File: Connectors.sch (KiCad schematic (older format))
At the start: 4 parts, among them J2 I2C connector, J3 Digital pins, J4 Serial connector, J5 ICSP connector

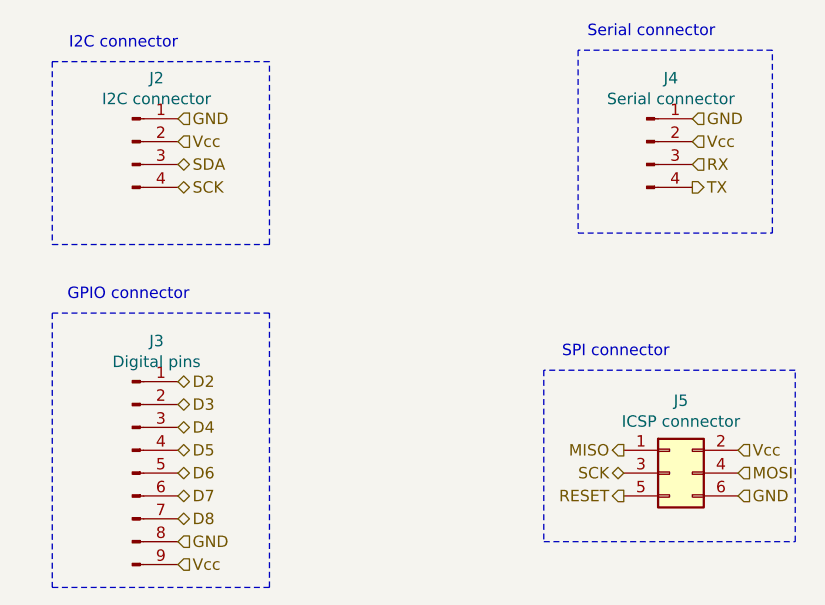
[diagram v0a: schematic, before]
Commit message: Adjusted designators, units etc as per Larry's feedback.
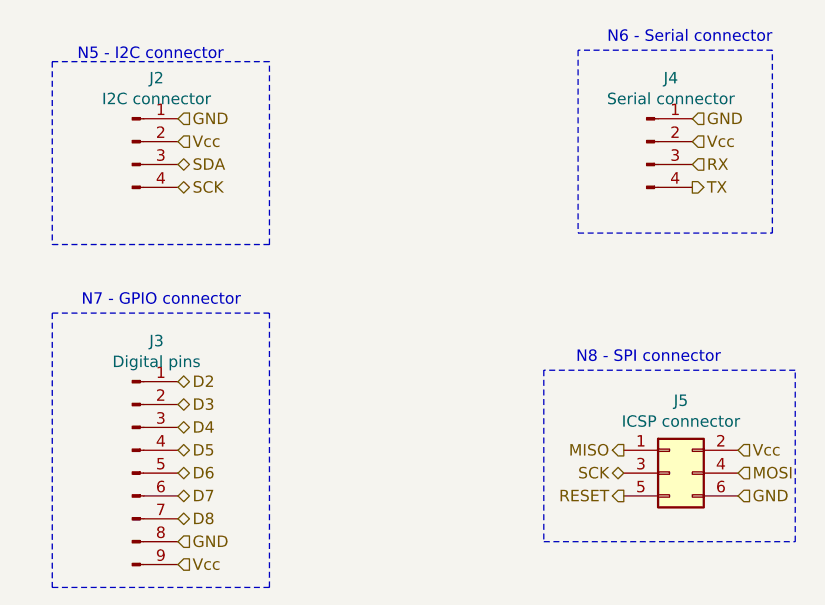
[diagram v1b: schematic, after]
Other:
- note added: "N5 - I2C connector"
- note added: "N6 - Serial connector"
- note added: "N7 - GPIO connector"
- note added: "N8 - SPI connector"
- note removed: "GPIO connector"
- note removed: "I2C connector"
- note removed: "SPI connector"
- note removed: "Serial connector"
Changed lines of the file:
@@
 EESchema Schematic File Version 4
+LIBS:BACEE-cache
 EELAYER 26 0
 EELAYER END
@@
 Wire Notes Line
 	6600 3500 5500 3500
-Text Notes 3900 2100 2    50   ~ 0
-I2C connector
-Text Notes 6250 2050 2    50   ~ 0
-Serial connector
-Text Notes 3950 3200 2    50   ~ 0
-GPIO connector
-Text Notes 6050 3450 2    50   ~ 0
-SPI connector
+Text Notes 4100 2150 2    50   ~ 0
+N5 - I2C connector
+Text Notes 6500 2075 2    50   ~ 0
+N6 - Serial connector
+Text Notes 4175 3225 2    50   ~ 0
+N7 - GPIO connector
+Text Notes 6275 3475 2    50   ~ 0
+N8 - SPI connector
 $EndSCHEMATC

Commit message: Adjusted designators, units etc as per Larry's feedback.
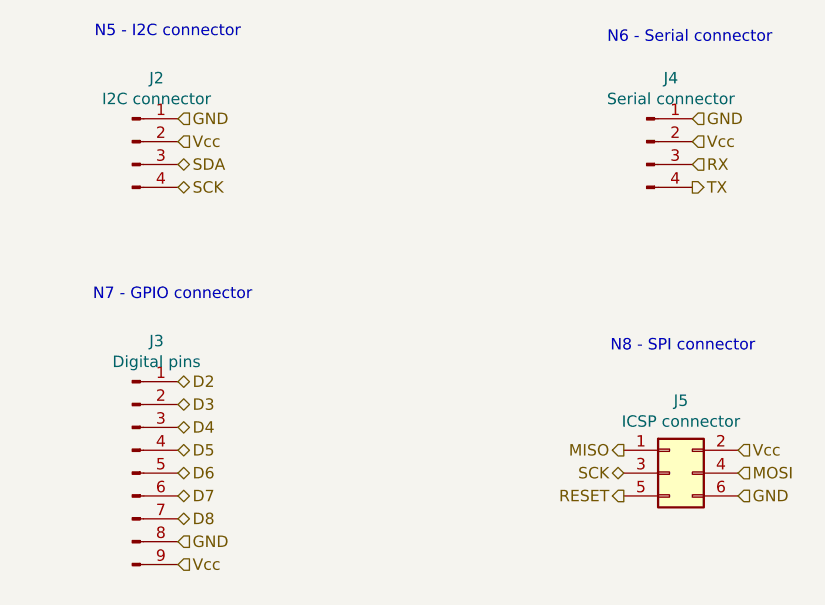
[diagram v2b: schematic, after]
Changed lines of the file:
@@
 Text HLabel 6150 2700 2    50   Output ~ 0
 TX
-Wire Notes Line
-	3350 2150 3350 2950
-Wire Notes Line
-	3350 2950 4300 2950
-Wire Notes Line
-	4300 2950 4300 2150
-Wire Notes Line
-	4300 2150 3350 2150
-Wire Notes Line
-	3350 3250 3350 4450
-Wire Notes Line
-	3350 4450 4300 4450
-Wire Notes Line
-	4300 4450 4300 3250
-Wire Notes Line
-	4300 3250 3350 3250
-Wire Notes Line
-	5650 2100 5650 2900
-Wire Notes Line
-	5650 2900 6500 2900
-Wire Notes Line
-	6500 2900 6500 2100
-Wire Notes Line
-	6500 2100 5650 2100
-Wire Notes Line
-	5500 3500 5500 4250
-Wire Notes Line
-	5500 4250 6600 4250
-Wire Notes Line
-	6600 4250 6600 3500
-Wire Notes Line
-	6600 3500 5500 3500
-Text Notes 4100 2150 2    50   ~ 0
+Text Notes 4175 2050 2    50   ~ 0
 N5 - I2C connector
 Text Notes 6500 2075 2    50   ~ 0
 N6 - Serial connector
-Text Notes 4175 3225 2    50   ~ 0
+Text Notes 4225 3200 2    50   ~ 0
 N7 - GPIO connector
-Text Notes 6275 3475 2    50   ~ 0
+Text Notes 6425 3425 2    50   ~ 0
 N8 - SPI connector
 $EndSCHEMATC
